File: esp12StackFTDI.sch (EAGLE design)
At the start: 35 parts, among them J02 470, J04 470, J05 470, J12 470, J13 470

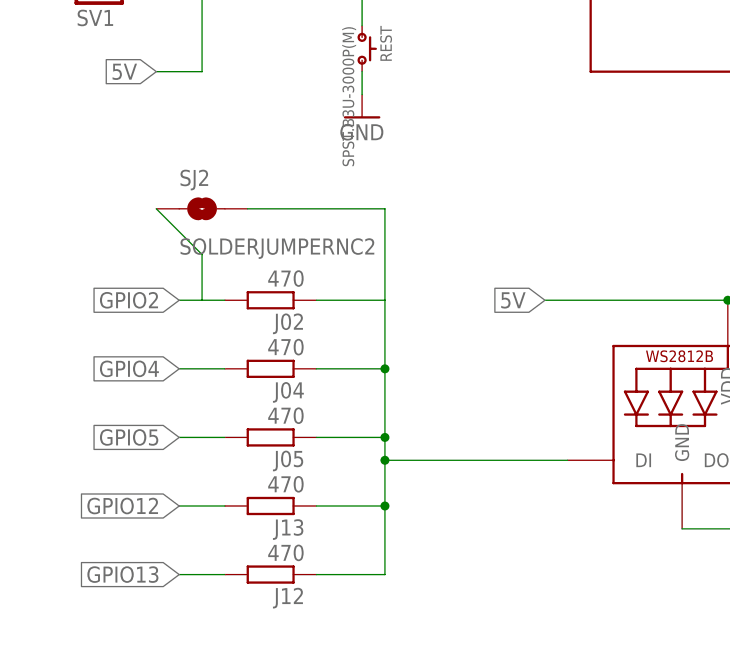
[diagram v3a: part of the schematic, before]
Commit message: initial test with solder jumpers
added solder jumpers instead of 0603 positions
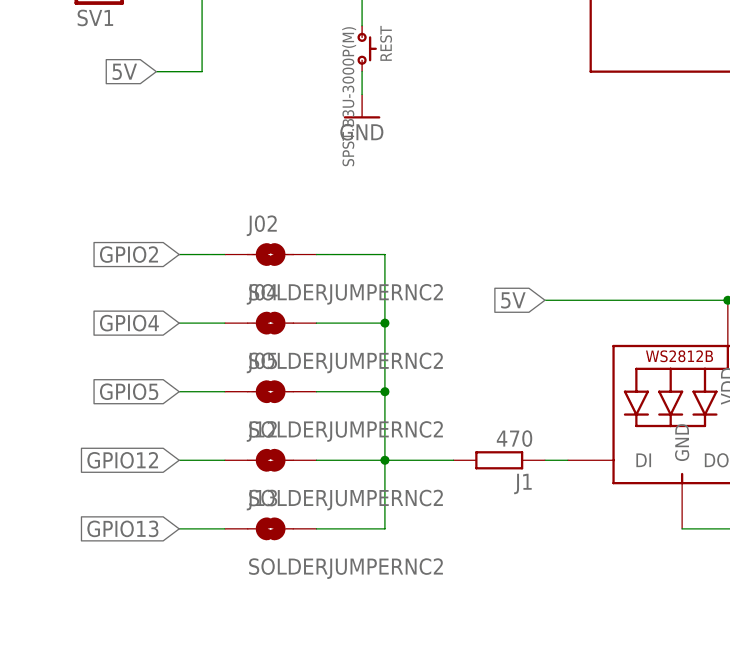
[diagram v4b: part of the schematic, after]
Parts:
- removed SJ2: SOLDERJUMPERNC2, SparkFun:SOLDERJUMPERNC2
- added J1: 470, eagle-ltspice:RR0603
- J02, J04, J05, J12, J13: value 470 -> SOLDERJUMPERNC2; device eagle-ltspice:RR0603 -> SparkFun:SOLDERJUMPERNC2
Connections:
- new net N$2: J1.1, LED1.DI
- net DIN1: now also J02.2, J04.2, J05.2, J1.2, J12.2, J13.2; no longer J02.1, J04.1, J05.1, J12.1, J13.1, LED1.DI, SJ2.2
- net GPIO12: now also J12.1; no longer J13.2
- net GPIO13: now also J13.1; no longer J12.2
- net GPIO2: now also J02.1; no longer J02.2, SJ2.1
- net GPIO4: now also J04.1; no longer J04.2
- net GPIO5: now also J05.1; no longer J05.2
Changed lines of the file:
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@@
 <part name="LED4" library="adafruit" deviceset="WS2812B" device="5050"/>
 <part name="GND2" library="supply1" deviceset="GND" device=""/>
-<part name="J05" library="eagle-ltspice" deviceset="R" device="R0603" value="470"/>
 <part name="GND6" library="supply1" deviceset="GND" device=""/>
-<part name="J04" library="eagle-ltspice" deviceset="R" device="R0603" value="470"/>
-<part name="J02" library="eagle-ltspice" deviceset="R" device="R0603" value="470"/>
-<part name="J13" library="eagle-ltspice" deviceset="R" device="R0603" value="470"/>
-<part name="J12" library="eagle-ltspice" deviceset="R" device="R0603" value="470"/>
 <part name="R10" library="eagle-ltspice" deviceset="R" device="R0603" value="4k7"/>
 <part name="R11" library="eagle-ltspice" deviceset="R" device="R0603" value="10k"/>
@@
 <part name="P+2" library="supply1" deviceset="VCC" device=""/>
 <part name="D1" library="adafruit" deviceset="DIODE" device="SOD-323F"/>
-<part name="SJ2" library="SparkFun" deviceset="SOLDERJUMPER" device="NC2"/>
+<part name="J02" library="SparkFun" deviceset="SOLDERJUMPER" device="NC2"/>
+<part name="J1" library="eagle-ltspice" deviceset="R" device="R0603" value="470"/>
+<part name="J04" library="SparkFun" deviceset="SOLDERJUMPER" device="NC2"/>
+<part name="J05" library="SparkFun" deviceset="SOLDERJUMPER" device="NC2"/>
+<part name="J12" library="SparkFun" deviceset="SOLDERJUMPER" device="NC2"/>
+<part name="J13" library="SparkFun" deviceset="SOLDERJUMPER" device="NC2"/>
 </parts>
 <sheets>
@@
 <instance part="LED4" gate="G$1" x="33.02" y="-50.8"/>
 <instance part="GND2" gate="1" x="58.42" y="-71.12"/>
-<instance part="J05" gate="G$1" x="-106.68" y="-50.8" rot="R180"/>
 <instance part="GND6" gate="1" x="-10.16" y="-20.32"/>
-<instance part="J04" gate="G$1" x="-106.68" y="-43.18" rot="R180"/>
-<instance part="J02" gate="G$1" x="-106.68" y="-35.56" rot="R180"/>
-<instance part="J13" gate="G$1" x="-106.68" y="-58.42" rot="R180"/>
-<instance part="J12" gate="G$1" x="-106.68" y="-66.04" rot="R180"/>
 <instance part="R10" gate="G$1" x="-38.1" y="101.6" rot="R270"/>
 <instance part="R11" gate="G$1" x="-38.1" y="78.74" rot="R270"/>
@@
 <instance part="P+2" gate="VCC" x="73.66" y="132.08"/>
 <instance part="D1" gate="G$1" x="-93.98" y="129.54"/>
-<instance part="SJ2" gate="1" x="-114.3" y="-25.4"/>
+<instance part="J02" gate="1" x="-106.68" y="-30.48"/>
+<instance part="J1" gate="G$1" x="-81.28" y="-53.34" rot="R180"/>
+<instance part="J04" gate="1" x="-106.68" y="-38.1"/>
+<instance part="J05" gate="1" x="-106.68" y="-45.72"/>
+<instance part="J12" gate="1" x="-106.68" y="-53.34"/>
+<instance part="J13" gate="1" x="-106.68" y="-60.96"/>
 </instances>
 <busses>
@@
 </segment>
 <segment>
-<pinref part="J13" gate="G$1" pin="2"/>
-<wire x1="-111.76" y1="-58.42" x2="-116.84" y2="-58.42" width="0.1524" layer="91"/>
-<label x="-116.84" y="-58.42" size="1.778" layer="95" rot="R180" xref="yes"/>
+<wire x1="-111.76" y1="-53.34" x2="-116.84" y2="-53.34" width="0.1524" layer="91"/>
+<label x="-116.84" y="-53.34" size="1.778" layer="95" rot="R180" xref="yes"/>
+<pinref part="J12" gate="1" pin="1"/>
 </segment>
 </net>
@@
 </segment>
 <segment>
-<pinref part="J05" gate="G$1" pin="2"/>
-<wire x1="-111.76" y1="-50.8" x2="-116.84" y2="-50.8" width="0.1524" layer="91"/>
-<label x="-116.84" y="-50.8" size="1.778" layer="95" rot="R180" xref="yes"/>
+<wire x1="-111.76" y1="-45.72" x2="-116.84" y2="-45.72" width="0.1524" layer="91"/>
+<label x="-116.84" y="-45.72" size="1.778" layer="95" rot="R180" xref="yes"/>
+<pinref part="J05" gate="1" pin="1"/>
 </segment>
 </net>
@@
 </segment>
 <segment>
-<pinref part="J02" gate="G$1" pin="2"/>
-<wire x1="-111.76" y1="-35.56" x2="-114.3" y2="-35.56" width="0.1524" layer="91"/>
-<label x="-116.84" y="-35.56" size="1.778" layer="95" rot="R180" xref="yes"/>
-<pinref part="SJ2" gate="1" pin="1"/>
-<wire x1="-114.3" y1="-35.56" x2="-116.84" y2="-35.56" width="0.1524" layer="91"/>
-<wire x1="-114.3" y1="-35.56" x2="-114.3" y2="-30.48" width="0.1524" layer="91"/>
-<wire x1="-114.3" y1="-30.48" x2="-119.38" y2="-25.4" width="0.1524" layer="91"/>
+<label x="-116.84" y="-30.48" size="1.778" layer="95" rot="R180" xref="yes"/>
+<wire x1="-111.76" y1="-30.48" x2="-116.84" y2="-30.48" width="0.1524" layer="91"/>
+<pinref part="J02" gate="1" pin="1"/>
 </segment>
 </net>
@@
 </segment>
 <segment>
-<pinref part="J04" gate="G$1" pin="2"/>
-<wire x1="-111.76" y1="-43.18" x2="-116.84" y2="-43.18" width="0.1524" layer="91"/>
-<label x="-116.84" y="-43.18" size="1.778" layer="95" rot="R180" xref="yes"/>
+<wire x1="-111.76" y1="-38.1" x2="-116.84" y2="-38.1" width="0.1524" layer="91"/>
+<label x="-116.84" y="-38.1" size="1.778" layer="95" rot="R180" xref="yes"/>
+<pinref part="J04" gate="1" pin="1"/>
 </segment>
 </net>
@@
 <pinref part="SV1" gate="1" pin="7"/>
 <wire x1="-76.2" y1="2.54" x2="-119.38" y2="2.54" width="0.1524" layer="91"/>
-<label x="-116.84" y="-66.04" size="1.778" layer="95" rot="R180" xref="yes"/>
-</segment>
-<segment>
-<pinref part="J12" gate="G$1" pin="2"/>
-<wire x1="-116.84" y1="-66.04" x2="-111.76" y2="-66.04" width="0.1524" layer="91"/>
+<label x="-116.84" y="-60.96" size="1.778" layer="95" rot="R180" xref="yes"/>
+</segment>
+<segment>
+<wire x1="-116.84" y1="-60.96" x2="-111.76" y2="-60.96" width="0.1524" layer="91"/>
+<pinref part="J13" gate="1" pin="1"/>
 </segment>
 </net>
@@
 <net name="DIN1" class="0">
 <segment>
-<pinref part="J02" gate="G$1" pin="1"/>
-<wire x1="-93.98" y1="-35.56" x2="-101.6" y2="-35.56" width="0.1524" layer="91"/>
-<pinref part="J04" gate="G$1" pin="1"/>
-<wire x1="-101.6" y1="-43.18" x2="-93.98" y2="-43.18" width="0.1524" layer="91"/>
-<pinref part="J12" gate="G$1" pin="1"/>
-<wire x1="-101.6" y1="-66.04" x2="-93.98" y2="-66.04" width="0.1524" layer="91"/>
-<wire x1="-93.98" y1="-66.04" x2="-93.98" y2="-58.42" width="0.1524" layer="91"/>
-<pinref part="J13" gate="G$1" pin="1"/>
-<wire x1="-101.6" y1="-58.42" x2="-93.98" y2="-58.42" width="0.1524" layer="91"/>
-<junction x="-93.98" y="-58.42"/>
-<wire x1="-93.98" y1="-58.42" x2="-93.98" y2="-53.34" width="0.1524" layer="91"/>
-<pinref part="J05" gate="G$1" pin="1"/>
-<wire x1="-93.98" y1="-53.34" x2="-93.98" y2="-50.8" width="0.1524" layer="91"/>
-<wire x1="-101.6" y1="-50.8" x2="-93.98" y2="-50.8" width="0.1524" layer="91"/>
-<junction x="-93.98" y="-50.8"/>
-<wire x1="-93.98" y1="-50.8" x2="-93.98" y2="-43.18" width="0.1524" layer="91"/>
-<junction x="-93.98" y="-43.18"/>
-<wire x1="-93.98" y1="-43.18" x2="-93.98" y2="-35.56" width="0.1524" layer="91"/>
-<pinref part="LED1" gate="G$1" pin="DI"/>
-<wire x1="-73.66" y1="-53.34" x2="-93.98" y2="-53.34" width="0.1524" layer="91"/>
+<wire x1="-93.98" y1="-30.48" x2="-101.6" y2="-30.48" width="0.1524" layer="91"/>
+<wire x1="-101.6" y1="-38.1" x2="-93.98" y2="-38.1" width="0.1524" layer="91"/>
+<wire x1="-101.6" y1="-60.96" x2="-93.98" y2="-60.96" width="0.1524" layer="91"/>
+<wire x1="-93.98" y1="-60.96" x2="-93.98" y2="-53.34" width="0.1524" layer="91"/>
+<wire x1="-101.6" y1="-53.34" x2="-93.98" y2="-53.34" width="0.1524" layer="91"/>
 <junction x="-93.98" y="-53.34"/>
-<pinref part="SJ2" gate="1" pin="2"/>
-<wire x1="-93.98" y1="-35.56" x2="-93.98" y2="-25.4" width="0.1524" layer="91"/>
-<wire x1="-93.98" y1="-25.4" x2="-109.22" y2="-25.4" width="0.1524" layer="91"/>
+<wire x1="-93.98" y1="-53.34" x2="-93.98" y2="-45.72" width="0.1524" layer="91"/>
+<wire x1="-101.6" y1="-45.72" x2="-93.98" y2="-45.72" width="0.1524" layer="91"/>
+<junction x="-93.98" y="-45.72"/>
+<wire x1="-93.98" y1="-45.72" x2="-93.98" y2="-38.1" width="0.1524" layer="91"/>
+<junction x="-93.98" y="-38.1"/>
+<wire x1="-93.98" y1="-38.1" x2="-93.98" y2="-30.48" width="0.1524" layer="91"/>
+<pinref part="J04" gate="1" pin="2"/>
+<pinref part="J02" gate="1" pin="2"/>
+<pinref part="J05" gate="1" pin="2"/>
+<pinref part="J12" gate="1" pin="2"/>
+<pinref part="J13" gate="1" pin="2"/>
+<pinref part="J1" gate="G$1" pin="2"/>
+<wire x1="-93.98" y1="-53.34" x2="-86.36" y2="-53.34" width="0.1524" layer="91"/>
 </segment>
 </net>
@@
 </segment>
 </net>
+<net name="N$2" class="0">
+<segment>
+<pinref part="J1" gate="G$1" pin="1"/>
+<pinref part="LED1" gate="G$1" pin="DI"/>
+<wire x1="-76.2" y1="-53.34" x2="-73.66" y2="-53.34" width="0.1524" layer="91"/>
+</segment>
+</net>

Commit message: optimizing solder jumpers
different placement for the solder jumpers
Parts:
- renumbered J1 to R8
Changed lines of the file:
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@@
 <part name="D1" library="adafruit" deviceset="DIODE" device="SOD-323F"/>
 <part name="J02" library="SparkFun" deviceset="SOLDERJUMPER" device="NC2"/>
-<part name="J1" library="eagle-ltspice" deviceset="R" device="R0603" value="470"/>
+<part name="R8" library="eagle-ltspice" deviceset="R" device="R0603" value="470"/>
 <part name="J04" library="SparkFun" deviceset="SOLDERJUMPER" device="NC2"/>
 <part name="J05" library="SparkFun" deviceset="SOLDERJUMPER" device="NC2"/>
@@
 <instance part="D1" gate="G$1" x="-93.98" y="129.54"/>
 <instance part="J02" gate="1" x="-106.68" y="-30.48"/>
-<instance part="J1" gate="G$1" x="-81.28" y="-53.34" rot="R180"/>
+<instance part="R8" gate="G$1" x="-81.28" y="-53.34" rot="R180"/>
 <instance part="J04" gate="1" x="-106.68" y="-38.1"/>
 <instance part="J05" gate="1" x="-106.68" y="-45.72"/>
@@
 <pinref part="J12" gate="1" pin="2"/>
 <pinref part="J13" gate="1" pin="2"/>
-<pinref part="J1" gate="G$1" pin="2"/>
+<pinref part="R8" gate="G$1" pin="2"/>
 <wire x1="-93.98" y1="-53.34" x2="-86.36" y2="-53.34" width="0.1524" layer="91"/>
 </segment>
@@
 <net name="N$2" class="0">
 <segment>
-<pinref part="J1" gate="G$1" pin="1"/>
+<pinref part="R8" gate="G$1" pin="1"/>
 <pinref part="LED1" gate="G$1" pin="DI"/>
 <wire x1="-76.2" y1="-53.34" x2="-73.66" y2="-53.34" width="0.1524" layer="91"/>

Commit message: some major updates
* working ft232rl layout
* replaced the DIN resistors for the WS2112 with solder jumpers
* sensors breakout board
* fixed a bug (missing trace) in the rgbwwpw board
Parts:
- removed J_REST: 10k, eagle-ltspice:RR0603
- added J01: SOLDERJUMPERNC2, SparkFun:SOLDERJUMPERNC2
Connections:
- net GPIO16: now also J01.1; no longer J_REST.1
- net REST: now also J01.2; no longer J_REST.2
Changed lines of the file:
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@@
 <part name="R10" library="eagle-ltspice" deviceset="R" device="R0603" value="4k7"/>
 <part name="R11" library="eagle-ltspice" deviceset="R" device="R0603" value="10k"/>
-<part name="J_REST" library="eagle-ltspice" deviceset="R" device="R0603" value="10k"/>
 <part name="U1" library="ftdichip-4" deviceset="FT232RL" device=""/>
 <part name="GND8" library="supply1" deviceset="GND" device=""/>
@@
 <part name="J12" library="SparkFun" deviceset="SOLDERJUMPER" device="NC2"/>
 <part name="J13" library="SparkFun" deviceset="SOLDERJUMPER" device="NC2"/>
+<part name="J01" library="SparkFun" deviceset="SOLDERJUMPER" device="NC2"/>
 </parts>
 <sheets>
@@
 <instance part="R10" gate="G$1" x="-38.1" y="101.6" rot="R270"/>
 <instance part="R11" gate="G$1" x="-38.1" y="78.74" rot="R270"/>
-<instance part="J_REST" gate="G$1" x="-111.76" y="30.48" rot="R90"/>
 <instance part="U1" gate="G$1" x="2.54" y="104.14"/>
 <instance part="GND8" gate="1" x="-2.54" y="55.88"/>
@@
 <instance part="J12" gate="1" x="-106.68" y="-53.34"/>
 <instance part="J13" gate="1" x="-106.68" y="-60.96"/>
+<instance part="J01" gate="1" x="-111.76" y="30.48" rot="R90"/>
 </instances>
 <busses>
@@
 <wire x1="-96.52" y1="17.78" x2="-96.52" y2="-5.08" width="0.1524" layer="91"/>
 <pinref part="REST" gate="G$1" pin="1"/>
-<pinref part="J_REST" gate="G$1" pin="2"/>
 <wire x1="-111.76" y1="35.56" x2="-106.68" y2="35.56" width="0.1524" layer="91"/>
 <wire x1="-106.68" y1="35.56" x2="-106.68" y2="17.78" width="0.1524" layer="91"/>
 <junction x="-106.68" y="17.78"/>
+<pinref part="J01" gate="1" pin="2"/>
 </segment>
 </net>
@@
 <pinref part="SV1" gate="1" pin="4"/>
 <wire x1="-76.2" y1="10.16" x2="-111.76" y2="10.16" width="0.1524" layer="91"/>
-<pinref part="J_REST" gate="G$1" pin="1"/>
 <wire x1="-111.76" y1="10.16" x2="-119.38" y2="10.16" width="0.1524" layer="91"/>
 <wire x1="-111.76" y1="10.16" x2="-111.76" y2="25.4" width="0.1524" layer="91"/>
 <junction x="-111.76" y="10.16"/>
-</segment>
-</net>
+<pinref part="J01" gate="1" pin="1"/>
+</segment>
+</net>
